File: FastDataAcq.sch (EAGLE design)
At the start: 215 parts, among them IC1 LT1963AEQ, IC2 FT230XQ, IC3 ADCMP553BRMZ, J1 MICRO-FIT_3.0_2POS_RA_SMD, J2 USB_MICROAB_SMT, X1 87832-14, X2 SMA-142-0701-801/806, X3 SMA-142-0701-801/806, Y1 SI530-500, Y2 100MHz, Y3 DNP

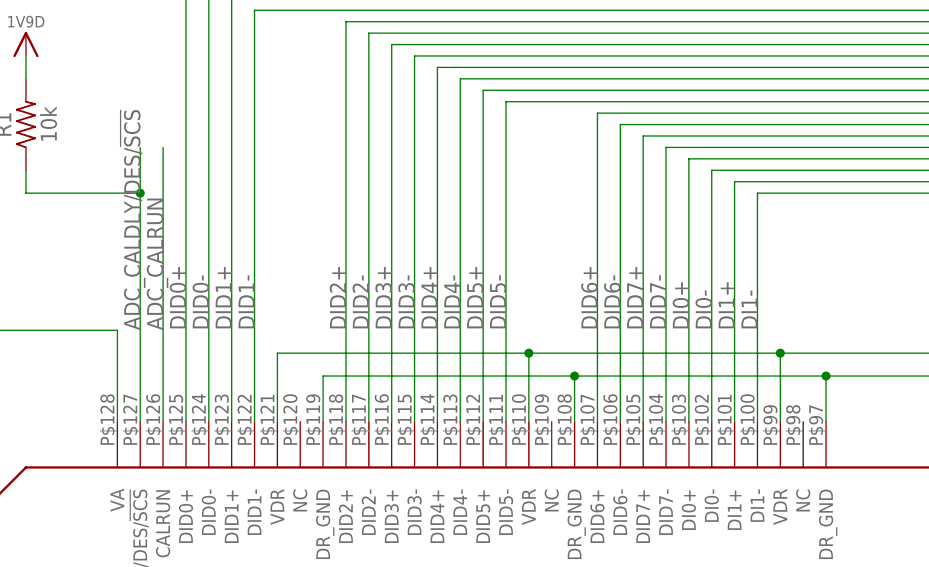
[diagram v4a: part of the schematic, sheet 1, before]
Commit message: LVDS Top Changed
Changed LVDS data lines to 5mil width and spacing. Bend separation is
25mil.  Only the top data lines are finished - still need to do the
bottom and sides.
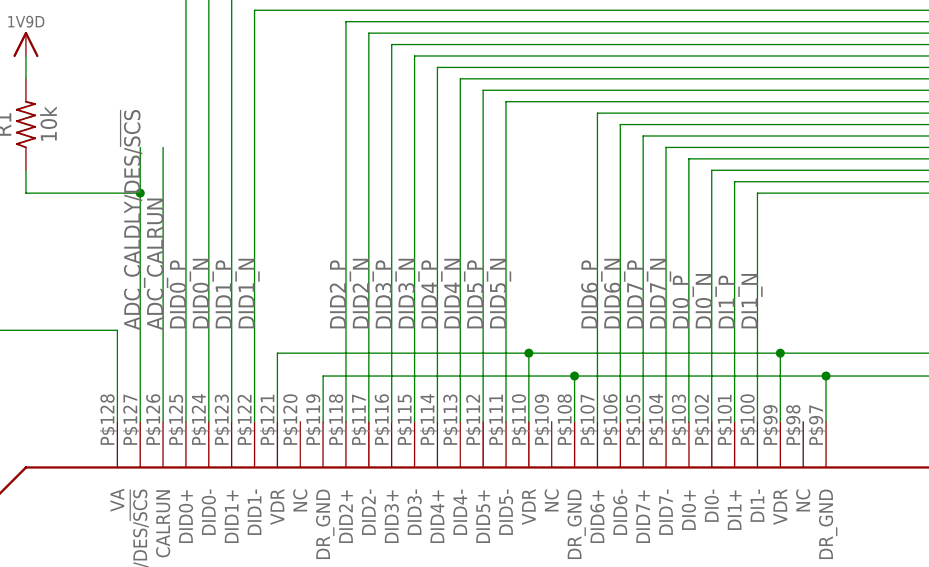
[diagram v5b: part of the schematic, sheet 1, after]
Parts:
- C7, C75: value NA -> DNP
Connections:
- net DI0+ renamed DI0_P
- net DI0- renamed DI0_N
- net DI1+ renamed DI1_P
- net DI1- renamed DI1_N
- net DID0+ renamed DID0_P
- net DID0- renamed DID0_N
- net DID1+ renamed DID1_P
- net DID1- renamed DID1_N
- net DID2+ renamed DID2_P
- net DID2- renamed DID2_N
- net DID3+ renamed DID3_P
- net DID3- renamed DID3_N
- net DID4+ renamed DID4_P
- net DID4- renamed DID4_N
- net DID5+ renamed DID5_P
- net DID5- renamed DID5_N
- net DID6+ renamed DID6_P
- net DID6- renamed DID6_N
- net DID7+ renamed DID7_P
- net DID7- renamed DID7_N
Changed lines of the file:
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@@
 <clearance class="2" value="0.1524"/>
+</class>
+<class number="3" name="LVDS_5" width="0.127" drill="0">
+<clearance class="3" value="0.127"/>
 </class>
 </classes>
@@
 <attribute name="SUPPLIER" value="DIGIKEY"/>
 </part>
-<part name="C75" library="rcl" deviceset="C-EU" device="C0603" value="NA">
+<part name="C75" library="rcl" deviceset="C-EU" device="C0603" value="DNP">
 <attribute name="PARTNUMBER" value=""/>
 <attribute name="SUPPLIER" value=""/>
 </part>
-<part name="C7" library="rcl" deviceset="C-EU" device="C0603" value="NA">
+<part name="C7" library="rcl" deviceset="C-EU" device="C0603" value="DNP">
 <attribute name="PARTNUMBER" value=""/>
 <attribute name="SUPPLIER" value=""/>
@@
 </busses>
 <nets>
-<net name="DI1-" class="0">
+<net name="DI1_N" class="3">
 <segment>
 <pinref part="U$1" gate="G$1" pin="DI1-"/>
@@
 </segment>
 </net>
-<net name="DI1+" class="0">
+<net name="DI1_P" class="3">
 <segment>
 <pinref part="U$1" gate="G$1" pin="DI1+"/>
@@
 </segment>
 </net>
-<net name="DI0-" class="0">
+<net name="DI0_N" class="3">
 <segment>
 <pinref part="U$1" gate="G$1" pin="DI0-"/>
@@
 </segment>
 </net>
-<net name="DI0+" class="0">
+<net name="DI0_P" class="3">
 <segment>
 <pinref part="U$1" gate="G$1" pin="DI0+"/>
@@
 </segment>
 </net>
-<net name="DID7-" class="0">
+<net name="DID7_N" class="3">
 <segment>
 <pinref part="U$1" gate="G$1" pin="DID7-"/>
@@
 </segment>
 </net>
-<net name="DID6-" class="0">
+<net name="DID6_N" class="3">
 <segment>
 <pinref part="U$1" gate="G$1" pin="DID6-"/>
@@
 </segment>
 </net>
-<net name="DID6+" class="0">
+<net name="DID6_P" class="3">
 <segment>
 <pinref part="U$1" gate="G$1" pin="DID6+"/>
@@
 </segment>
 </net>
-<net name="DID5-" class="0">
+<net name="DID5_N" class="3">
 <segment>
 <pinref part="U$1" gate="G$1" pin="DID5-"/>
@@
 </segment>
 </net>
-<net name="DID5+" class="0">
+<net name="DID5_P" class="3">
 <segment>
 <pinref part="U$1" gate="G$1" pin="DID5+"/>
@@
 </segment>
 </net>
-<net name="DID4-" class="0">
+<net name="DID4_N" class="3">
 <segment>
 <pinref part="U$1" gate="G$1" pin="DID4-"/>
@@
 </segment>
 </net>
-<net name="DID4+" class="0">
+<net name="DID4_P" class="3">
 <segment>
 <pinref part="U$1" gate="G$1" pin="DID4+"/>
@@
 </segment>
 </net>
-<net name="DID3-" class="0">
+<net name="DID3_N" class="3">
 <segment>
 <pinref part="U$1" gate="G$1" pin="DID3-"/>
@@
 </segment>
 </net>
-<net name="DID3+" class="0">
+<net name="DID3_P" class="3">
 <segment>
 <wire x1="119.38" y1="247.65" x2="307.34" y2="247.65" width="0.1524" layer="91"/>
@@
 </segment>
 </net>
-<net name="DID2-" class="0">
+<net name="DID2_N" class="3">
 <segment>
 <pinref part="U$1" gate="G$1" pin="DID2-"/>
@@
 </segment>
 </net>
-<net name="DID2+" class="0">
+<net name="DID2_P" class="3">
 <segment>
 <pinref part="U$1" gate="G$1" pin="DID2+"/>
@@
 </segment>
 </net>
-<net name="DID1-" class="0">
+<net name="DID1_N" class="3">
 <segment>
 <pinref part="U$1" gate="G$1" pin="DID1-"/>
@@
 </segment>
 </net>
-<net name="DID1+" class="0">
+<net name="DID1_P" class="3">
 <segment>
 <pinref part="U$1" gate="G$1" pin="DID1+"/>
@@
 </segment>
 </net>
-<net name="DID0-" class="0">
+<net name="DID0_N" class="3">
 <segment>
 <pinref part="U$1" gate="G$1" pin="DID0-"/>
@@
 </segment>
 </net>
-<net name="DID0+" class="0">
+<net name="DID0_P" class="3">
 <segment>
 <pinref part="U$1" gate="G$1" pin="DID0+"/>
@@
 </segment>
 </net>
-<net name="DID7+" class="0">
+<net name="DID7_P" class="3">
 <segment>
 <pinref part="U$1" gate="G$1" pin="DID7+"/>

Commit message: Partially done with LVDS bottom half.
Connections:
- net DQ0+ renamed DQ0_P
- net DQ0- renamed DQ0_N
- net DQ1+ renamed DQ1_P
- net DQ1- renamed DQ1_N
- net DQ2+ renamed DQ2_P
- net DQ2- renamed DQ2_N
- net DQD0+ renamed DQD0_P
- net DQD0- renamed DQD0_N
- net DQD1+ renamed DQD1_P
- net DQD1- renamed DQD1_N
- net DQD2+ renamed DQD2_P
- net DQD2- renamed DQD2_N
- net DQD3+ renamed DQD3_P
- net DQD3- renamed DQD3_N
- net DQD4+ renamed DQD4_P
- net DQD4- renamed DQD4_N
- net DQD5+ renamed DQD5_P
- net DQD5- renamed DQD5_N
- net DQD6+ renamed DQD6_P
- net DQD6- renamed DQD6_N
- net DQD7+ renamed DQD7_P
- net DQD7- renamed DQD7_N
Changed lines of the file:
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@@
 </segment>
 </net>
-<net name="ADC_DCLK_N" class="1">
+<net name="ADC_DCLK_N" class="3">
 <segment>
 <pinref part="U$1" gate="G$1" pin="DCLK-"/>
@@
 </segment>
 </net>
-<net name="ADC_DCLK_P" class="1">
+<net name="ADC_DCLK_P" class="3">
 <segment>
 <pinref part="U$1" gate="G$1" pin="DCLK+"/>
@@
 </segment>
 </net>
-<net name="DI7_N" class="1">
+<net name="DI7_N" class="3">
 <segment>
 <pinref part="U$2" gate="G$1" pin="IO_L37P_GCLK13_0"/>
@@
 </segment>
 </net>
-<net name="DI7_P" class="1">
+<net name="DI7_P" class="3">
 <segment>
 <pinref part="U$1" gate="G$1" pin="DI7+"/>
@@
 </segment>
 </net>
-<net name="DI6_N" class="1">
+<net name="DI6_N" class="3">
 <segment>
 <pinref part="U$2" gate="G$1" pin="IO_L62P_0"/>
@@
 </segment>
 </net>
-<net name="DI6_P" class="1">
+<net name="DI6_P" class="3">
 <segment>
 <pinref part="U$1" gate="G$1" pin="DI6+"/>
@@
 </segment>
 </net>
-<net name="DI5_N" class="1">
+<net name="DI5_N" class="3">
 <segment>
 <pinref part="U$1" gate="G$1" pin="DI5-"/>
@@
 </segment>
 </net>
-<net name="DI5_P" class="1">
+<net name="DI5_P" class="3">
 <segment>
 <pinref part="U$1" gate="G$1" pin="DI5+"/>
@@
 </segment>
 </net>
-<net name="DI4_N" class="1">
+<net name="DI4_N" class="3">
 <segment>
 <pinref part="U$1" gate="G$1" pin="DI4-"/>
@@
 </segment>
 </net>
-<net name="DI4_P" class="1">
+<net name="DI4_P" class="3">
 <segment>
 <pinref part="U$1" gate="G$1" pin="DI4+"/>
@@
 </segment>
 </net>
-<net name="DI3_N" class="1">
+<net name="DI3_N" class="3">
 <segment>
 <pinref part="U$1" gate="G$1" pin="DI3-"/>
@@
 </segment>
 </net>
-<net name="DI3_P" class="1">
+<net name="DI3_P" class="3">
 <segment>
 <pinref part="U$1" gate="G$1" pin="DI3+"/>
@@
 </segment>
 </net>
-<net name="DI2_N" class="1">
+<net name="DI2_N" class="3">
 <segment>
 <pinref part="U$1" gate="G$1" pin="DI2-"/>
@@
 </segment>
 </net>
-<net name="DI2_P" class="1">
+<net name="DI2_P" class="3">
 <segment>
 <pinref part="U$1" gate="G$1" pin="DI2+"/>
@@
 </segment>
 </net>
-<net name="DQ7_P" class="1">
+<net name="DQ7_P" class="3">
 <segment>
 <pinref part="U$1" gate="G$1" pin="DQ7-"/>
@@
 </segment>
 </net>
-<net name="DQ7_N" class="1">
+<net name="DQ7_N" class="3">
 <segment>
 <pinref part="U$1" gate="G$1" pin="DQ7+"/>
@@
 </segment>
 </net>
-<net name="DQ6_P" class="1">
+<net name="DQ6_P" class="3">
 <segment>
 <pinref part="U$1" gate="G$1" pin="DQ6-"/>
@@
 </segment>
 </net>
-<net name="DQ6_N" class="1">
+<net name="DQ6_N" class="3">
 <segment>
 <pinref part="U$1" gate="G$1" pin="DQ6+"/>
@@
 </segment>
 </net>
-<net name="DQ5_P" class="1">
+<net name="DQ5_P" class="3">
 <segment>
 <pinref part="U$1" gate="G$1" pin="DQ5-"/>
@@
 </segment>
 </net>
-<net name="DQ5_N" class="1">
+<net name="DQ5_N" class="3">
 <segment>
 <pinref part="U$2" gate="G$1" pin="IO_L4P_0"/>
@@
 </segment>
 </net>
-<net name="DQ4_P" class="1">
+<net name="DQ4_P" class="3">
 <segment>
 <pinref part="U$1" gate="G$1" pin="DQ4-"/>
@@
 </segment>
 </net>
-<net name="DQ4_N" class="1">
+<net name="DQ4_N" class="3">
 <segment>
 <pinref part="U$2" gate="G$1" pin="IO_L3P_0"/>
@@
 </segment>
 </net>
-<net name="DQ3_P" class="1">
+<net name="DQ3_P" class="3">
 <segment>
 <pinref part="U$1" gate="G$1" pin="DQ3-"/>
@@
 </segment>
 </net>
-<net name="DQ3_N" class="1">
+<net name="DQ3_N" class="3">
 <segment>
 <pinref part="U$1" gate="G$1" pin="DQ3+"/>
@@
 </segment>
 </net>
-<net name="DQ2-" class="0">
+<net name="DQ2_N" class="3">
 <segment>
 <pinref part="U$1" gate="G$1" pin="DQ2-"/>
@@
 </segment>
 </net>
-<net name="DQ2+" class="0">
+<net name="DQ2_P" class="3">
 <segment>
 <pinref part="U$1" gate="G$1" pin="DQ2+"/>
@@
 </segment>
 </net>
-<net name="DQ1-" class="0">
+<net name="DQ1_N" class="3">
 <segment>
 <pinref part="U$1" gate="G$1" pin="DQ1-"/>
@@
 </segment>
 </net>
-<net name="DQ1+" class="0">
+<net name="DQ1_P" class="3">
 <segment>
 <pinref part="U$2" gate="G$1" pin="IO_L52P_3"/>
@@
 </segment>
 </net>
-<net name="DQ0-" class="0">
+<net name="DQ0_N" class="3">
 <segment>
 <pinref part="U$1" gate="G$1" pin="DQ0-"/>
@@
 </segment>
 </net>
-<net name="DQ0+" class="0">
+<net name="DQ0_P" class="3">
 <segment>
 <pinref part="U$2" gate="G$1" pin="IO_L51P_3"/>
@@
 </segment>
 </net>
-<net name="DQD7-" class="0">
+<net name="DQD7_N" class="3">
 <segment>
 <pinref part="U$1" gate="G$1" pin="DQD7-"/>
@@
 </segment>
 </net>
-<net name="DQD7+" class="0">
+<net name="DQD7_P" class="3">
 <segment>
 <pinref part="U$2" gate="G$1" pin="IO_L50P_3"/>
@@
 </segment>
 </net>
-<net name="DQD6-" class="0">
+<net name="DQD6_N" class="3">
 <segment>
 <pinref part="U$1" gate="G$1" pin="DQD6-"/>
@@
 </segment>
 </net>
-<net name="DQD6+" class="0">
+<net name="DQD6_P" class="3">
 <segment>
 <pinref part="U$2" gate="G$1" pin="IO_L49P_3"/>
@@
 </segment>
 </net>
-<net name="DQD5-" class="0">
+<net name="DQD5_N" class="3">
 <segment>
 <wire x1="132.08" y1="88.9" x2="132.08" y2="58.42" width="0.1524" layer="91"/>
@@
 </segment>
 </net>
-<net name="DQD5+" class="0">
+<net name="DQD5_P" class="3">
 <segment>
 <pinref part="U$2" gate="G$1" pin="IO_L44P_GCLK21_3"/>
@@
 </segment>
 </net>
-<net name="DQD4-" class="0">
+<net name="DQD4_N" class="3">
 <segment>
 <pinref part="U$2" gate="G$1" pin="IO_L43N_GCLK22_IRDY2_3"/>
@@
 </segment>
 </net>
-<net name="DQD4+" class="0">
+<net name="DQD4_P" class="3">
 <segment>
 <pinref part="U$1" gate="G$1" pin="DQD4+"/>
@@
 </segment>
 </net>
-<net name="DQD3-" class="0">
+<net name="DQD3_N" class="3">
 <segment>
 <pinref part="U$2" gate="G$1" pin="IO_L42N_GCLK24_3"/>
@@
 </segment>
 </net>
-<net name="DQD3+" class="0">
+<net name="DQD3_P" class="3">
 <segment>
 <pinref part="U$1" gate="G$1" pin="DQD3+"/>
@@
 </segment>
 </net>
-<net name="DQD2-" class="0">
+<net name="DQD2_N" class="3">
 <segment>
 <pinref part="U$2" gate="G$1" pin="IO_L41N_GCLK26_3"/>
@@
 </segment>
 </net>
-<net name="DQD2+" class="0">
+<net name="DQD2_P" class="3">
 <segment>
 <pinref part="U$1" gate="G$1" pin="DQD2+"/>
@@
 </segment>
 </net>
-<net name="DQD1-" class="0">
+<net name="DQD1_N" class="3">
 <segment>
 <pinref part="U$2" gate="G$1" pin="IO_L37N_3"/>
@@
 </segment>
 </net>
-<net name="DQD1+" class="0">
+<net name="DQD1_P" class="3">
 <segment>
 <pinref part="U$1" gate="G$1" pin="DQD1+"/>
@@
 </segment>
 </net>
-<net name="DQD0-" class="0">
+<net name="DQD0_N" class="3">
 <segment>
 <pinref part="U$2" gate="G$1" pin="IO_L36N_3"/>
@@
 </segment>
 </net>
-<net name="DQD0+" class="0">
+<net name="DQD0_P" class="3">
 <segment>
 <pinref part="U$1" gate="G$1" pin="DQD0+"/>

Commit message: Finished LVDS layout.
Making additional final changes. Still need to add test points.
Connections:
- net ADC_CLK+ renamed ADC_CLK_P
- net ADC_CLK- renamed ADC_CLK_N
- net CLK500+ renamed CLK500_P
- net CLK500- renamed CLK500_N
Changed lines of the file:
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@@
 <class number="0" name="default" width="0" drill="0">
 </class>
-<class number="1" name="LVDS" width="0.1524" drill="0">
-<clearance class="1" value="0.1016"/>
+<class number="1" name="50_Ohm" width="0.2794" drill="0">
+<clearance class="1" value="0.254"/>
 </class>
 <class number="2" name="Power" width="0" drill="0">
@@
 </segment>
 </net>
-<net name="ADC_VINI-" class="0">
+<net name="ADC_VINI-" class="1">
 <segment>
 <pinref part="U$1" gate="G$1" pin="VINI-"/>
@@
 </segment>
 </net>
-<net name="ADC_VINI+" class="0">
+<net name="ADC_VINI+" class="1">
 <segment>
 <pinref part="U$1" gate="G$1" pin="VINI+"/>
@@
 </segment>
 </net>
-<net name="ADC_CLK+" class="0">
+<net name="ADC_CLK_P" class="0">
 <segment>
 <pinref part="U$1" gate="G$1" pin="CLK+"/>
@@
 </segment>
 </net>
-<net name="ADC_CLK-" class="0">
+<net name="ADC_CLK_N" class="0">
 <segment>
 <pinref part="U$1" gate="G$1" pin="CLK-"/>
@@
 </segment>
 </net>
-<net name="CLK500-" class="0">
+<net name="CLK500_N" class="3">
 <segment>
 <pinref part="Y1" gate="G$1" pin="CLK-"/>
@@
 </segment>
 </net>
-<net name="CLK500+" class="0">
+<net name="CLK500_P" class="3">
 <segment>
 <pinref part="Y1" gate="G$1" pin="CLK+"/>
@@
 </segment>
 </net>
-<net name="ADC_CLK-" class="0">
+<net name="ADC_CLK_N" class="0">
 <segment>
 <pinref part="C82" gate="G$1" pin="2"/>
@@
 </segment>
 </net>
-<net name="ADC_CLK+" class="0">
+<net name="ADC_CLK_P" class="0">
 <segment>
 <pinref part="C79" gate="G$1" pin="2"/>
@@
 </segment>
 </net>
-<net name="ADC_VINI+" class="0">
+<net name="ADC_VINI+" class="1">
 <segment>
 <pinref part="U$10" gate="G$1" pin="VOUT+"/>
@@
 </segment>
 </net>
-<net name="ADC_VINI-" class="0">
+<net name="ADC_VINI-" class="1">
 <segment>
 <pinref part="U$10" gate="G$1" pin="VOUT-"/>
@@
 </segment>
 </net>
-<net name="SIGNAL_IN" class="0">
+<net name="SIGNAL_IN" class="1">
 <segment>
 <pinref part="U$10" gate="G$1" pin="VIN+"/>

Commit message: Parts finalized. Layout near done.
Still a few things on the to do list, but most tracks are final. Still
need test points and to go over all text that's getting printed.
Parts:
- removed R64: 523K, rcl:R-US_R0201
- removed U$95: HEADER_0.1"_8P_2R_SMT, Schuyler:HEADER_0.1"_8P_2R_SMT
- added R58: 0, rcl:R-US_R0603
- added X4: 87832-14, con-molex:87832-14
- C10, C11, C14, C27, C28, C29: value .1uF -> 10pF; device Schuyler:CAPACITOR0204_REVERSE -> rcl:C-EUC0201; PARTNUMBER 587-2152-1-ND -> 445-1769-1-ND; SUPPLIER DIGIKEY -> (none)
- C101, C103, C84, C86: value 10nF -> .1uF; device rcl:C-EUC0201 -> Schuyler:CAPACITOR0204_REVERSE; PARTNUMBER 445-1793-1-ND -> 587-2152-1-ND; SUPPLIER (none) -> DIGIKEY
- C102, C81: value 1uF -> .1uF; PARTNUMBER 445-9091-1-ND -> 587-2152-1-ND
- C104, C87, C90: value .1uF -> 1uF; PARTNUMBER 587-2152-1-ND -> 445-9091-1-ND
- C105: value DNP -> 4.7uF; device rcl:C-EUC0603 -> Schuyler:CAPACITOR; MANPARTNUMBER (none) -> CL05A475MQ5NRNC; MANUFACTURER (none) -> Samsung Electro-Mechanics America, Inc; PARTNUMBER (none) -> 1276-1056-1-ND
- C12, C13, C15, C30, C83: value .1uF -> 33uF; device Schuyler:CAPACITOR0204_REVERSE -> SparkFun-Passives:CAP0805; PARTNUMBER 587-2152-1-ND -> 445-8238-1-ND; SUPPLIER DIGIKEY -> (none)
- C16, C17, C22, C8: value .1uF -> 10uF; device Schuyler:CAPACITOR0204_REVERSE -> rcl:C-EUC0603; PARTNUMBER 587-2152-1-ND -> 445-4112-1-ND
- C19, C3: value 33uF -> 10uF; device SparkFun-Passives:CAP0805 -> rcl:C-EUC0603; PARTNUMBER 445-8238-1-ND -> 445-4112-1-ND; SUPPLIER (none) -> DIGIKEY
- C2: value 10pF -> 10uF; device rcl:C-EUC0201 -> rcl:C-EUC0603; PARTNUMBER 445-1769-1-ND -> 445-4112-1-ND; SUPPLIER (none) -> DIGIKEY
- C20: value 100uF -> 10uF; device Schuyler:CAP_POL_D9_SERIES -> rcl:C-EUC0603; MANPARTNUMBER ECASD91B107M012K00 -> (none); PARTNUMBER 490-5480-1-ND -> 445-4112-1-ND; SUPPLIER (none) -> DIGIKEY
- C23, C9: value .1uF -> DNP; device Schuyler:CAPACITOR0204_REVERSE -> rcl:C-EUC0603; PARTNUMBER 587-2152-1-ND -> (none); SUPPLIER DIGIKEY -> (none)
- C24, C25, C26: value .1uF -> 22uF 150mOhm ESR; device Schuyler:CAPACITOR0204_REVERSE -> rcl:C-USC0805; PARTNUMBER 587-2152-1-ND -> P16231CT-ND
- C32: value 10uF -> 33uF; device rcl:C-EUC0603 -> SparkFun-Passives:CAP0805; PARTNUMBER 445-4112-1-ND -> 445-8238-1-ND; SUPPLIER DIGIKEY -> (none)
- C33, C66: value 10pF -> 4.7uF; device rcl:C-EUC0201 -> Schuyler:CAPACITOR; MANPARTNUMBER (none) -> CL05A475MQ5NRNC; MANUFACTURER (none) -> Samsung Electro-Mechanics America, Inc; PARTNUMBER 445-1769-1-ND -> 1276-1056-1-ND; SUPPLIER (none) -> DIGIKEY
- C34, C74: value 33uF -> 4.7uF; device SparkFun-Passives:CAP0805 -> Schuyler:CAPACITOR; MANPARTNUMBER (none) -> CL05A475MQ5NRNC; MANUFACTURER (none) -> Samsung Electro-Mechanics America, Inc; PARTNUMBER 445-8238-1-ND -> 1276-1056-1-ND; SUPPLIER (none) -> DIGIKEY
- C35, C36, C41: MANPARTNUMBER (none) -> CL05A475MQ5NRNC; MANUFACTURER (none) -> Samsung Electro-Mechanics America, Inc; PARTNUMBER (none) -> 1276-1056-1-ND; SUPPLIER (none) -> DIGIKEY
- C37, C42, C43, C62: value 4.7uF -> 0.47uF; device Schuyler:CAPACITOR -> Schuyler:CAPACITOR0204_REVERSE; PARTNUMBER (none) -> 1276-1779-1-ND; SUPPLIER (none) -> DIGIKEY
- C39, C40: value 4.7uF -> 33uF; device Schuyler:CAPACITOR -> SparkFun-Passives:CAP0805; PARTNUMBER (none) -> 445-8238-1-ND
- C44, C45, C47, C50, C59: value 4.7uF -> .1uF; device Schuyler:CAPACITOR -> Schuyler:CAPACITOR0204_REVERSE; PARTNUMBER (none) -> 587-2152-1-ND; SUPPLIER (none) -> DIGIKEY
- C48, C49, C60, C64: value 0.47uF -> .1uF; PARTNUMBER 1276-1779-1-ND -> 587-2152-1-ND
- C5: value 10pF -> DNP; device rcl:C-EUC0201 -> rcl:C-EUC0603; PARTNUMBER 445-1769-1-ND -> (none)
- C51, C52, C61: value 0.47uF -> 4.7uF; device Schuyler:CAPACITOR0204_REVERSE -> Schuyler:CAPACITOR; MANPARTNUMBER (none) -> CL05A475MQ5NRNC; MANUFACTURER (none) -> Samsung Electro-Mechanics America, Inc; PARTNUMBER 1276-1779-1-ND -> 1276-1056-1-ND
- C53, C72: value 10uF -> 4.7uF; device rcl:C-EUC0603 -> Schuyler:CAPACITOR; MANPARTNUMBER (none) -> CL05A475MQ5NRNC; MANUFACTURER (none) -> Samsung Electro-Mechanics America, Inc; PARTNUMBER 445-4112-1-ND -> 1276-1056-1-ND
- C54, C71: value 10pF -> .1uF; device rcl:C-EUC0201 -> Schuyler:CAPACITOR0204_REVERSE; PARTNUMBER 445-1769-1-ND -> 587-2152-1-ND; SUPPLIER (none) -> DIGIKEY
- C55, C67, C91: value 33uF -> .1uF; device SparkFun-Passives:CAP0805 -> Schuyler:CAPACITOR0204_REVERSE; PARTNUMBER 445-8238-1-ND -> 587-2152-1-ND; SUPPLIER (none) -> DIGIKEY
- C56, C58: value 10uF -> 0.47uF; device rcl:C-EUC0603 -> Schuyler:CAPACITOR0204_REVERSE; PARTNUMBER 445-4112-1-ND -> 1276-1779-1-ND
- C57, C69: value 22uF 150mOhm ESR -> 4.7uF; device rcl:C-USC0805 -> Schuyler:CAPACITOR; MANPARTNUMBER (none) -> CL05A475MQ5NRNC; MANUFACTURER (none) -> Samsung Electro-Mechanics America, Inc; PARTNUMBER P16231CT-ND -> 1276-1056-1-ND
- C6: value 33uF -> 100uF; device SparkFun-Passives:CAP0805 -> Schuyler:CAP_POL_D9_SERIES; MANPARTNUMBER (none) -> ECASD91B107M012K00; PARTNUMBER 445-8238-1-ND -> 490-5480-1-ND
- C65, C68, C70: value 10uF -> .1uF; device rcl:C-EUC0603 -> Schuyler:CAPACITOR0204_REVERSE; PARTNUMBER 445-4112-1-ND -> 587-2152-1-ND
- C7, C75: value DNP -> .1uF; device rcl:C-EUC0603 -> Schuyler:CAPACITOR0204_REVERSE; PARTNUMBER (none) -> 587-2152-1-ND; SUPPLIER (none) -> DIGIKEY
- C73: value 22uF 150mOhm ESR -> .1uF; device rcl:C-USC0805 -> Schuyler:CAPACITOR0204_REVERSE; PARTNUMBER P16231CT-ND -> 587-2152-1-ND
- C76: value 10nF -> 0.47uF; device rcl:C-EUC0201 -> Schuyler:CAPACITOR0204_REVERSE; PARTNUMBER 445-1793-1-ND -> 1276-1779-1-ND; SUPPLIER (none) -> DIGIKEY
- C77: value .1uF -> 100pF; device Schuyler:CAPACITOR0204_REVERSE -> rcl:C-EUC0201; PARTNUMBER 587-2152-1-ND -> 445-4675-1-ND
- C78: value 1uF -> 4.7nF; device Schuyler:CAPACITOR0204_REVERSE -> rcl:C-EUC0201; PARTNUMBER 445-9091-1-ND -> 445-13726-1-ND; SUPPLIER DIGIKEY -> (none)
- C79: PARTNUMBER 445-1795-1-ND -> 445-13726-1-ND
- C82: value 4.7nF -> .1uF; device rcl:C-EUC0201 -> Schuyler:CAPACITOR0204_REVERSE; PARTNUMBER 445-1795-1-ND -> 587-2152-1-ND; SUPPLIER (none) -> DIGIKEY
- C85, C94, C97: value .1uF -> 10nF; device Schuyler:CAPACITOR0204_REVERSE -> rcl:C-EUC0201; PARTNUMBER 587-2152-1-ND -> 445-1793-1-ND; SUPPLIER DIGIKEY -> (none)
- C88: value 100pF -> 33uF; device rcl:C-EUC0201 -> SparkFun-Passives:CAP0805; PARTNUMBER 445-4675-1-ND -> 445-8238-1-ND; SUPPLIER DIGIKEY -> (none)
- C89: value .1uF -> 4.7uF; device Schuyler:CAPACITOR0204_REVERSE -> Schuyler:CAPACITOR; MANPARTNUMBER (none) -> CL05A475MQ5NRNC; MANUFACTURER (none) -> Samsung Electro-Mechanics America, Inc; PARTNUMBER 587-2152-1-ND -> 1276-1056-1-ND
- C92: value 4.7uF -> .1uF; device Schuyler:CAPACITOR0304_REVERSE -> Schuyler:CAPACITOR0204_REVERSE; PARTNUMBER 445-13745-1-ND -> 587-2152-1-ND
- C93: value 4.7uF -> 10nF; device Schuyler:CAPACITOR -> rcl:C-EUC0201; PARTNUMBER (none) -> 445-1793-1-ND
- C98: value 33uF -> 10nF; device SparkFun-Passives:CAP0805 -> rcl:C-EUC0201; PARTNUMBER 445-8238-1-ND -> 445-1793-1-ND
- D1, D4: PARTNUMBER (none) -> LNJ237W82RACT-ND
- L1: value 2.2uH -> CHOKE_CM_ACM7060-301; device Schuyler:INDUCTOR_3X3.6 -> Schuyler:CHOKE_CM_ACM7060-301; PARTNUMBER 541-1322-1-ND -> (none); SUPPLIER DIGIKEY -> (none)
- L10, L9: value 2.2uH -> 26; device Schuyler:INDUCTOR_3X3.6 -> Schuyler:FERRITE_BEADS_BLM18SG260; PARTNUMBER 541-1322-1-ND -> (none); SUPPLIER DIGIKEY -> (none)
- L2: value CHOKE_CM_ACM7060-301 -> 26; device Schuyler:CHOKE_CM_ACM7060-301 -> Schuyler:FERRITE_BEADS_BLM18SG260
- L3: device Schuyler:INDUCTOR_5.18X5.49 -> Schuyler:INDUCTOR_3X3.6; PARTNUMBER 541-1220-1-ND -> 541-1322-1-ND
- L4, L6: value 26 -> 2.2uH; device Schuyler:FERRITE_BEADS_BLM18SG260 -> Schuyler:INDUCTOR_3X3.6; PARTNUMBER (none) -> 541-1322-1-ND; SUPPLIER (none) -> DIGIKEY
- L5: value 26 -> 2.2uH; device Schuyler:FERRITE_BEADS_BLM18SG260 -> Schuyler:INDUCTOR_5.18X5.49; PARTNUMBER (none) -> 541-1220-1-ND; SUPPLIER (none) -> DIGIKEY
- R1, R6: value 10k -> DNP; device rcl:R-US_R0201 -> rcl:R-US_R0603; MANPARTNUMBER RC0603J103CS -> (none); MANUFACTURER Samsung Electro-Mechanics America, Inc -> (none); PARTNUMBER 1276-3817-1-ND -> (none); SUPPLIER DIGIKEY -> (none)
- R10, R16: value 210K -> 523K; PARTNUMBER P210KABCT-ND -> P523KABCT-ND
- R11: value 422K -> 649K; PARTNUMBER P442KABCT-ND -> P649KABCT-ND
- R12: value 10k -> 150K; MANPARTNUMBER RC0603J103CS -> (none); MANUFACTURER Samsung Electro-Mechanics America, Inc -> (none); PARTNUMBER 1276-3817-1-ND -> 1276-3719-1-ND
- R13, R17: value 270k -> 523K; PARTNUMBER P270KABCT-ND -> P523KABCT-ND
- R14: value 330 -> 523K; MANPARTNUMBER RC0603J331CS -> (none); MANUFACTURER Samsung Electro-Mechanics America, Inc -> (none); PARTNUMBER 1276-3787-1-ND -> P523KABCT-ND
- R15: value 845k -> 113k; PARTNUMBER P845KABCT-ND -> P113KABCT-ND
- R18, R28: value 523K -> 210K; PARTNUMBER P523KABCT-ND -> P210KABCT-ND
- R19: value 806K -> 150K; PARTNUMBER P806KABCT-ND -> 1276-3719-1-ND
- R20: value 649K -> 523K; PARTNUMBER P649KABCT-ND -> P523KABCT-ND
- R21: value 523K -> 10k; MANPARTNUMBER (none) -> RC0603J103CS; MANUFACTURER (none) -> Samsung Electro-Mechanics America, Inc; PARTNUMBER P523KABCT-ND -> 1276-3817-1-ND
- R22: value 1.15k 1% -> 280K; device rcl:R-US_R0603 -> rcl:R-US_R0201; MANPARTNUMBER RC1608F1151CS -> (none); MANUFACTURER Samsung Electro-Mechanics America, Inc -> (none); PARTNUMBER 1276-4649-1-ND -> P280KABCT-ND
- R24: value 280K -> 523K; PARTNUMBER P280KABCT-ND -> P523KABCT-ND
- R25: value 100 -> 523K; device rcl:R-US_R0603 -> rcl:R-US_R0201; MANPARTNUMBER RC1608J101CS -> (none); MANUFACTURER Samsung Electro-Mechanics America, Inc -> (none); PARTNUMBER 1276-5038-1-ND -> P523KABCT-ND
- R26: value 2k 1% -> DNP; MANPARTNUMBER RC1608F202CS -> (none); MANUFACTURER Samsung Electro-Mechanics America, Inc -> (none); PARTNUMBER 1276-3495-1-ND -> (none); SUPPLIER DIGIKEY -> (none)
- R27: value 523K -> 270k; PARTNUMBER P523KABCT-ND -> P270KABCT-ND
- R29: value 210K -> 1.15k 1%; device rcl:R-US_R0201 -> rcl:R-US_R0603; MANPARTNUMBER (none) -> RC1608F1151CS; MANUFACTURER (none) -> Samsung Electro-Mechanics America, Inc; PARTNUMBER P210KABCT-ND -> 1276-4649-1-ND
- R3, R8: value DNP -> 10k; device rcl:R-US_R0603 -> rcl:R-US_R0201; MANPARTNUMBER (none) -> RC0603J103CS; MANUFACTURER (none) -> Samsung Electro-Mechanics America, Inc; PARTNUMBER (none) -> 1276-3817-1-ND; SUPPLIER (none) -> DIGIKEY
- R30: value 649K -> 2k 1%; device rcl:R-US_R0201 -> rcl:R-US_R0603; MANPARTNUMBER (none) -> RC1608F202CS; MANUFACTURER (none) -> Samsung Electro-Mechanics America, Inc; PARTNUMBER P649KABCT-ND -> 1276-3495-1-ND
- R31: value 523K -> 100; device rcl:R-US_R0201 -> rcl:R-US_R0603; MANPARTNUMBER (none) -> RC1608J101CS; MANUFACTURER (none) -> Samsung Electro-Mechanics America, Inc; PARTNUMBER P523KABCT-ND -> 1276-5038-1-ND
- R32: value 150K -> 806K; PARTNUMBER 1276-3719-1-ND -> P806KABCT-ND
- R33: value 150K -> 210K; PARTNUMBER 1276-3719-1-ND -> P210KABCT-ND
- R34: value 523K -> 649K; PARTNUMBER P523KABCT-ND -> P649KABCT-ND
- R35: value 100 0.1% -> 845k; device rcl:R-US_R0402 -> rcl:R-US_R0201; MANPARTNUMBER ERA-2AEB101X -> (none); MANUFACTURER Panasonic Electronic Components -> (none); PARTNUMBER P100DCCT-ND -> P845KABCT-ND
- R36: value 100 0.1% -> 422K; device rcl:R-US_R0402 -> rcl:R-US_R0201; MANPARTNUMBER ERA-2AEB101X -> (none); MANUFACTURER Panasonic Electronic Components -> (none); PARTNUMBER P100DCCT-ND -> P442KABCT-ND
- R37: value 4.7k -> 270k; MANPARTNUMBER ERJ-1GNJ472C -> (none); MANUFACTURER Panasonic Electronic Components -> (none); PARTNUMBER P4.7AECT-ND -> P270KABCT-ND
- R39: value 0 -> 50; device rcl:R-US_R0603 -> rcl:R-US_R0201; MANPARTNUMBER (none) -> RC0603F49R9C; MANUFACTURER (none) -> Samsung Electro-Mechanics America, Inc; PARTNUMBER 311-0.0GRCT-ND -> 1276-3590-1-ND
- R40: value DNP -> 50; device rcl:R-US_R0603 -> rcl:R-US_R0201; MANPARTNUMBER (none) -> RC0603F49R9C; MANUFACTURER (none) -> Samsung Electro-Mechanics America, Inc; PARTNUMBER 311-0.0GRCT-ND -> 1276-3590-1-ND
- R41: value 113k -> 10k; MANPARTNUMBER (none) -> RC0603J103CS; MANUFACTURER (none) -> Samsung Electro-Mechanics America, Inc; PARTNUMBER P113KABCT-ND -> 1276-3817-1-ND
- R42: value 330 -> 26.1k; device rcl:R-US_R0201 -> rcl:R-US_R0603; MANPARTNUMBER RC0603J331CS -> (none); MANUFACTURER Samsung Electro-Mechanics America, Inc -> (none); PARTNUMBER 1276-3787-1-ND -> 1276-4779-1-ND
- R43, R44, R47: value 330 -> 10k; MANPARTNUMBER RC0603J331CS -> RC0603J103CS; PARTNUMBER 1276-3787-1-ND -> 1276-3817-1-ND
- R46: value 330 -> 16k; device rcl:R-US_R0201 -> rcl:R-US_R0603; MANPARTNUMBER RC0603J331CS -> (none); MANUFACTURER Samsung Electro-Mechanics America, Inc -> (none); PARTNUMBER 1276-3787-1-ND -> 1276-5091-1-ND
- R49: value 10k -> 330; MANPARTNUMBER RC0603J103CS -> RC0603J331CS; PARTNUMBER 1276-3817-1-ND -> 1276-3787-1-ND
- R50: value 10k -> 50; MANPARTNUMBER RC0603J103CS -> RC0603F49R9C; PARTNUMBER 1276-3817-1-ND -> 1276-3590-1-ND
- R52: value 27 -> 50; MANPARTNUMBER (none) -> RC0603F49R9C; MANUFACTURER (none) -> Samsung Electro-Mechanics America, Inc; PARTNUMBER 1276-3577-1-ND -> 1276-3590-1-ND
- R53: value 27 -> 100 0.1%; device rcl:R-US_R0201 -> rcl:R-US_R0402; MANPARTNUMBER (none) -> ERA-2AEB101X; MANUFACTURER (none) -> Panasonic Electronic Components; PARTNUMBER 1276-3577-1-ND -> P100DCCT-ND
- R54: value 26.1k -> 100 0.1%; device rcl:R-US_R0603 -> rcl:R-US_R0402; MANPARTNUMBER (none) -> ERA-2AEB101X; MANUFACTURER (none) -> Panasonic Electronic Components; PARTNUMBER 311-0.0GRCT-ND -> P100DCCT-ND
- R55: value 16k -> 330; device rcl:R-US_R0603 -> rcl:R-US_R0201; MANPARTNUMBER (none) -> RC0603J331CS; MANUFACTURER (none) -> Samsung Electro-Mechanics America, Inc; PARTNUMBER 311-0.0GRCT-ND -> 1276-3787-1-ND
- R56, R57: value 10k -> 330; device rcl:R-US_R0603 -> rcl:R-US_R0201; MANPARTNUMBER (none) -> RC0603J331CS; MANUFACTURER (none) -> Samsung Electro-Mechanics America, Inc; PARTNUMBER 311-0.0GRCT-ND -> 1276-3787-1-ND
- R59: value 50 -> 4.7k; MANPARTNUMBER RC0603F49R9C -> ERJ-1GNJ472C; MANUFACTURER Samsung Electro-Mechanics America, Inc -> Panasonic Electronic Components; PARTNUMBER 1276-3590-1-ND -> P4.7AECT-ND
- R60, R61: value 50 -> 27; MANPARTNUMBER RC0603F49R9C -> (none); MANUFACTURER Samsung Electro-Mechanics America, Inc -> (none); PARTNUMBER 1276-3590-1-ND -> 1276-3577-1-ND
- R62: value 50 -> 330; MANPARTNUMBER RC0603F49R9C -> RC0603J331CS; PARTNUMBER 1276-3590-1-ND -> 1276-3787-1-ND
- R63: value 523K -> 330; MANPARTNUMBER (none) -> RC0603J331CS; MANUFACTURER (none) -> Samsung Electro-Mechanics America, Inc; PARTNUMBER P523KABCT-ND -> 1276-3787-1-ND
- R7: value 4.7k -> 3.3k 0.1%; device rcl:R-US_R0201 -> rcl:R-US_R0603; MANPARTNUMBER ERJ-1GNJ472C -> (none); MANUFACTURER Panasonic Electronic Components -> (none); PARTNUMBER P4.7AECT-ND -> P3.3KDBCT-ND
- R9: value 3.3k 0.1% -> 4.7k; device rcl:R-US_R0603 -> rcl:R-US_R0201; MANPARTNUMBER (none) -> ERJ-1GNJ472C; MANUFACTURER (none) -> Panasonic Electronic Components; PARTNUMBER P3.3KDBCT-ND -> P4.7AECT-ND
- X1: value 87832-14 -> SMA-142-0701-801/806; device con-molex:87832-14 -> con-coax:SMA-142-0701-801/806; MANPARTNUMBER (none) -> 142-0701-801; MANUFACTURER (none) -> Emerson Network Power Connectivity Johnson; PARTNUMBER 57J0374 -> J502-ND; SUPPLIER Newark -> DIGIKEY
- X3: value SMA-142-0701-801/806 -> HEADER_0.1"_8P_2R_SMT; device con-coax:SMA-142-0701-801/806 -> Schuyler:HEADER_0.1"_8P_2R_SMT; MANPARTNUMBER 142-0701-801 -> (none); MANUFACTURER Emerson Network Power Connectivity Johnson -> (none); PARTNUMBER J502-ND -> (none); SUPPLIER DIGIKEY -> (none)
- renumbered IC1 to U6, IC2 to U14, IC3 to U12, U$1 to U1, U$10 to U8, U$11 to U9, U$14 to U3, U$2 to U2, U$4 to U7, U$5 to U4, U$6 to U5, U$7 to U13, U$8 to U10, U$9 to U11
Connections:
- removed net FPGA_TRIG+: R57.2, R61.2, U12.QA, U2.IO_L31P_GCLK31_D14_2
- removed net FPGA_TRIG-: R56.2, R60.2, U12.!QA, U2.IO_L31N_GCLK30_D15_2
- new net FPGA_TRIG_N: R47.2, R50.2, U12.!QA, U2.IO_L31N_GCLK30_D15_2
- new net FPGA_TRIG_P: R43.2, R52.2, U12.QA, U2.IO_L31P_GCLK31_D14_2
- net !PB: now also X3.P$5; no longer U$95.P$5
- net 1V2: now also C28.1, C31.1, C33.1, C41.1, C46.1, L7.P$2, R27.1, R33.2; no longer C2.1, C3.1, C35.1, C37.1, C38.1, L1.P$2, R10.2, R13.1
- net 1V8: now also C27.1, C30.1, C38.1, C42.1, C56.1, C58.1, L6.P$2, R21.2, R32.2; no longer C33.1, C47.1, C48.1, C49.1, C50.1, C64.1, L7.P$2, R12.2, R19.2
- net 1V9: now also C26.1, L10.P$1, L9.P$1, R29.2, R31.2; no longer C57.1, L4.P$1, L6.P$1, R22.2, R25.2
- net 1V9A: now also C39.1, C44.1, C47.2, C49.2, C54.1, C59.1, C64.2, C67.1, C70.1, C73.2, C75.1, L9.P$2, R3.1, R6.2; no longer C10.2, C11.1, C12.1, C13.2, C14.1, C15.1, C16.2, C17.1, C19.1, C8.1, C9.2, L4.P$2, R6.1, R8.2
- net 1V9D: now also C40.1, C45.1, C48.1, C50.1, C55.1, C60.1, C65.1, C68.1, C71.1, L10.P$2, R8.2; no longer C22.1, C23.1, C24.1, C25.1, C26.1, C27.1, C28.1, C29.1, C31.1, L6.P$2, R2.2
- net 2V3_1V9PRE: now also C14.1, C15.1, C19.1, L5.P$2, R20.2; no longer C54.1, C55.1, C56.1, L8.P$2, R21.2
- net 2V5: now also C24.1, L12.P$2; no longer C69.1, L11.P$2
- net 2V5A: now also C85.1, C86.1, C87.1, L12.P$1; no longer C76.1, C77.1, C78.1, L11.P$1
- net 2V8_2V5PRE: now also C10.1, C12.1, C16.1, L3.P$2, R11.1, R16.2; no longer C66.1, C67.1, C68.1, L9.P$2, R27.2, R30.1
- net 3V3: now also C104.1, C29.1, C32.1, C35.1, C37.1, C53.1, C57.1, C66.1, C69.1, C72.1, C74.1, C76.1, C88.1, C89.1, C90.1, C91.1, C92.1, C96.1, C97.1, L8.P$2, R23.2, R25.2, R38.1, R41.2, R44.2, R45.1, R48.1, R49.1, R53.2, R55.2, R59.2, R9.2, X3.P$7, X4.2; no longer C103.1, C39.1, C40.1, C41.1, C42.1, C44.1, C45.1, C46.1, C5.1, C59.1, C6.1, C60.1, C80.1, C81.1, C83.1, C85.1, C86.1, C87.1, C98.1, L3.P$2, R14.1, R15.2, R37.2, R38.2, R42.1, R43.1, R44.1, R49.2, R50.2, R63.2, R64.2, R7.2, U$95.P$7, X1.2
- net 3V3A: now also C25.1, L11.P$2; no longer C73.1, L12.P$2
- net 3V3OUT: now also C101.2, R62.1, R63.1; no longer C96.2, R45.1, R46.1
- net 3V3S: now also C80.1, C81.1, C82.1, C83.1, L11.P$1; no longer C104.1, C89.1, C90.1, C91.1, L12.P$1
- net 3V6_PRE3V3: now also C11.1, C13.1, C17.1, L4.P$2, R17.2; no longer C71.1, C72.1, C74.1, L10.P$2, R31.2
- net 5VUSB: now also C103.2, C105.2; no longer C92.1, C97.2
- net 5VUSB_CON: now also C98.1; no longer C101.1
- net ADC_CAL: now also R3.2; no longer R6.2
- net ADC_CALDLY/DES/!SCS: now also R8.1; no longer R1.1
- net ADC_CLK_N: now also C79.2; no longer C82.2
- net ADC_CLK_P: now also C78.2; no longer C79.2
- net ADC_FSR/ECE: now also R1.1, R2.2; no longer R2.1, R3.2
- net ADC_PWR_EN: now also R14.2; no longer R23.2
- net ADC_REXT: now also R7.2; no longer R9.2
- net ADC_TDIODE+: now also C77.1; no longer C88.1
- net ADC_TDIODE-: now also C77.2; no longer C88.2
- net ADC_VBG: now also R6.1; no longer R8.1
- net ANALOG_PWR_EN: now also R10.2; no longer R28.2
- net CLK500_N: now also C78.1; no longer C79.1
- net CLK500_P: now also C79.1; no longer C82.1
- net FPGA_CCLK: now also R53.1, R54.2; no longer R35.1, R36.2
- net FPGA_DONE: now also R55.1; no longer R38.1
- net FPGA_GPIO1: now also X3.P$4; no longer U$95.P$4
- net FPGA_GPIO2: now also X3.P$2; no longer U$95.P$2
- net FPGA_GPIO3: now also X3.P$1; no longer U$95.P$1
- net FPGA_GPIO4: now also X3.P$3; no longer U$95.P$3
- net FPGA_INITB: now also R59.1; no longer R37.1
- net FPGA_PROGRAMB: now also R58.2, R9.1; no longer R39.2, R7.1
- net FPGA_RXD: now also R56.2; no longer R47.2
- net FPGA_SCL: now also R41.1; no longer R50.1
- net FPGA_SDA: now also R44.1; no longer R49.1
- net FPGA_TCK: now also X4.6; no longer X1.6
- net FPGA_TDI: now also X4.10; no longer X1.10
- net FPGA_TMS: now also X4.4; no longer X1.4
- net FPGA_TXD: now also R57.2; no longer R48.2
- net FTDI_RXD: now also R57.1; no longer R48.1
- net FTDI_TXD: now also R56.1; no longer R47.1
- net GND: now also C101.1, C103.1, C105.1, C13.2, C16.2, C2.2, C20.2, C33.2, C47.1, C49.1, C5.2, C54.2, C6.NEG, C64.1, C66.2, C71.2, C73.1, C82.2, C88.2, C9.2, C96.2, C97.2, L1.P$4, R10.1, R12.2, R14.1, R15.1, R19.1, R2.1, R22.1, R30.1, R31.1, R34.1, R37.1, R39.1, R40.1, R54.1, R7.1, X1.2, X3.P$8, X4.1, X4.11, X4.13, X4.3, X4.5, X4.7, X4.9; no longer C10.1, C101.2, C103.2, C105.2, C11.2, C13.1, C14.2, C16.1, C20.NEG, C27.2, C28.2, C29.2, C47.2, C49.2, C6.2, C64.2, C73.2, C77.2, C78.2, C9.1, C96.1, C97.1, L2.P$4, R11.1, R16.1, R17.1, R20.1, R23.1, R25.1, R26.1, R29.1, R3.1, R32.2, R33.1, R41.1, R59.1, R62.1, R9.1, U$95.P$8, X1.1, X1.11, X1.13, X1.3, X1.5, X1.7, X1.9, X3.2
- net N$1: now also R38.2; no longer R14.2
- net N$10: now also R62.2; no longer R45.2
- net N$11: now also R58.1; no longer R39.1
- net N$12: now also R13.1, R15.2; no longer R34.1, R41.2
- net N$13: now also R63.2; no longer R46.2
- net N$14: now also R29.1, R30.2; no longer R22.1, R26.2
- net N$15: now also R42.2, R43.1; no longer R54.2, R57.1
- net N$17: now also C9.1; no longer C105.1
- net N$18: now also R50.1, R51.2, R52.1; no longer R60.1, R61.1, R62.2
- net N$19: now also R49.2; no longer R44.2
- net N$2: now also R39.2; no longer R51.2
- net N$20: now also R46.2, R47.1; no longer R55.2, R56.1
- net N$21: now also R48.2; no longer R43.2
- net N$22: now also R45.2; no longer R42.2
- net N$24: now also C6.POS, L1.P$3, L2.P$1; no longer C20.POS, L2.P$3, L5.P$1
- net N$3: now also R60.2; no longer R52.2
- net N$34: now also L1.P$1; no longer L2.P$1
- net N$35: now also L1.P$2; no longer L2.P$2
- net N$4: now also R60.1; no longer R52.1
- net N$5: now also R61.1; no longer R53.1
- net N$6: now also R13.2; no longer R34.2
- net N$7: now also R61.2; no longer R53.2
- net PGOOD: now also R21.1; no longer R12.1
- net PROM_TDO: now also X4.8; no longer X1.8
- net PWR_INT: now also R23.1; no longer R64.1
- net PWR_KILL: now also R25.1; no longer R63.1
- net S1EN: now also C23.1, R27.2, R28.2; no longer C7.1, R13.2, R16.2
- net S1FB: now also C29.2, R35.1, R37.2; no longer C5.2, R15.1, R17.2
- net S1SW: now also L8.P$1; no longer L3.P$1
- net S3EN: now also C5.1, R11.2, R12.1; no longer C75.1, R30.2, R32.1
- net S3FB: now also C11.2, R17.1, R19.2; no longer C71.2, R31.1, R33.2
- net S3SW: now also L4.P$1; no longer L10.P$1
- net S4FB: now also C27.2, R32.1, R34.2; no longer C33.2, R19.1, R20.2
- net S4SW: now also L6.P$1; no longer L7.P$1
- net S5FB: now also C14.2, R20.1, R22.2; no longer C54.2, R21.1, R24.2
- net S5SW: now also L5.P$1; no longer L8.P$1
- net S7FB: now also C28.2, R33.1, R36.2; no longer C2.2, R10.1, R11.2
- net S7SW: now also L7.P$1; no longer L1.P$1
- net S8FB: now also C10.2, R16.1, R18.2; no longer C66.2, R27.1, R29.2
- net S8SW: now also L3.P$1; no longer L9.P$1
- net SIGNAL_IN: now also X1.1; no longer X2.1
- net S_MODE: now also R24.2, R26.2; no longer R18.2, R40.2
- net S_TEMP: now also X3.P$6; no longer U$95.P$6
- net TRIGGER: now also R40.2, X2.1; no longer R59.2, X3.1
- net TRIG_RESET_HIGH: now also R46.1; no longer R55.1
- net TRIG_RESET_LOW: now also R42.1; no longer R54.1
- net VIN: now also C2.1, C20.1, C22.1, C3.1, C7.1, C8.1, L2.P$2, R26.1; no longer C30.1, C32.1, C53.1, C58.1, C65.1, C70.1, L5.P$2, R40.1
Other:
- note added: "Blue"
- note added: "Green"
- note added: "NOTE: !CF! used by JTAG to reset FPGA. If wrong, desolder resistor."
- note added: "Red"
- note removed: "NOTE: !CF! used to by JTAG to reset FPGA. If wrong, desolder resistor."
- moved on the sheet: C1, C10, C101, C102, C103, C104, C11, C12, C13, C14, C15, C16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
